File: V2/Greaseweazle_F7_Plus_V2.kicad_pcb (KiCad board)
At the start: 2 copper layers, 80 x 50 mm, 77 parts, among them J1 Wurth 694106301002, J10 PIN1X2, J11 PIN1X2, J12 IDC Box Header, J2 USB_B, J3 Molex 105017-1001, J4 TE EI 171826-4, J5 PIN1X3, J6 PIN1X2, J7 PIN1X5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

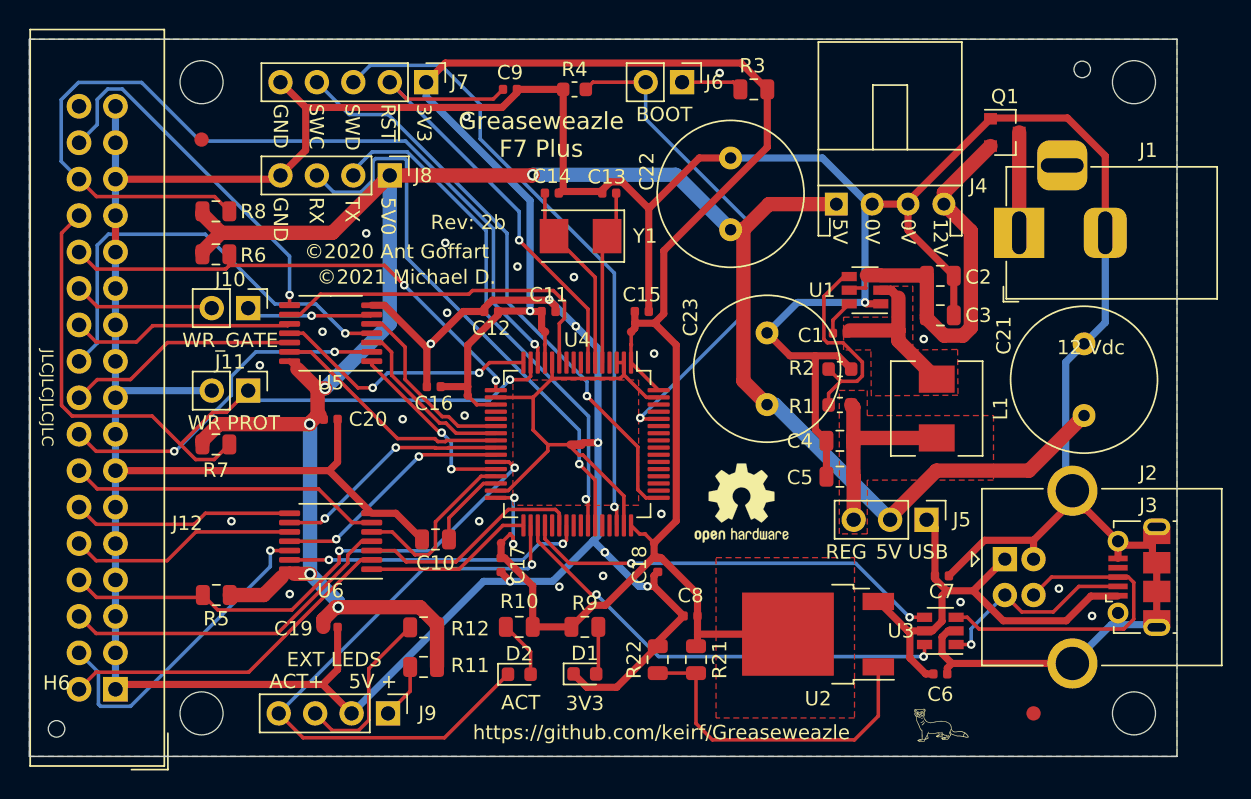
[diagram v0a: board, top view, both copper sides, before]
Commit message: moved U11 NarrowPowCon to get better routing
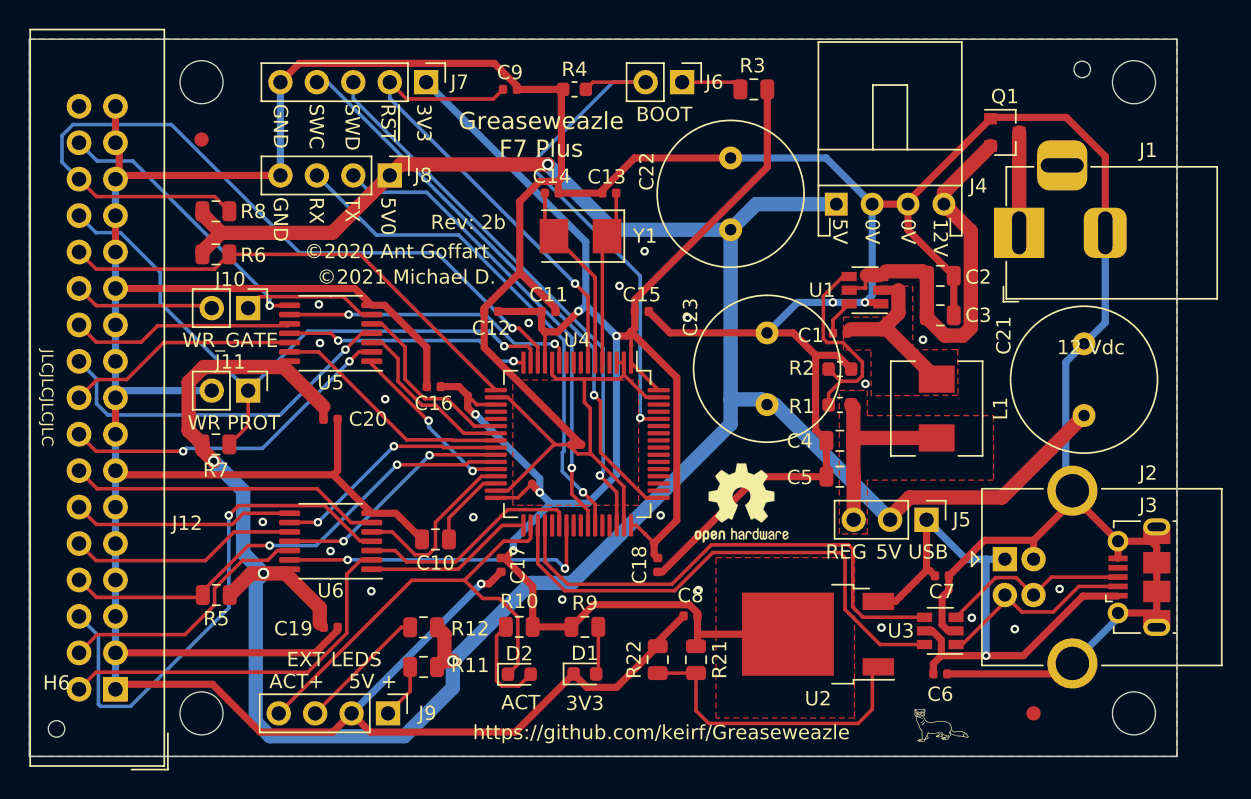
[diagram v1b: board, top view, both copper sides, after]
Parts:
- LOGO2: value Greaseweazle Logo -> GW Logo
- moved U11 4.67 mm to (185.0, 131.0), turned to 315 degrees
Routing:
- net GND: track 389.5 -> 434.8 mm, vias 30 -> 23
- net +5V: track 156.2 -> 192.1 mm, vias 5 -> 4
- net /~PIN6_5V~: track 23.9 -> 36.4 mm, vias 0 -> 1
- net /ACT: track 43.2 -> 32.6 mm, vias 1 -> 0
- net /~WR_PROT~: track 55.3 -> 45.2 mm
- net /USB_DIN+: track 23.2 -> 13.5 mm
- net /~RD_DAT~: track 62.9 -> 55.9 mm
- net /USB_VBUS: track 34.0 -> 40.0 mm, vias 0 -> 1
- net /~SIDE_5V~: track 25.5 -> 19.7 mm
- net /~STEP_5V~: track 30.9 -> 25.3 mm
- net /USB_D+: track 29.7 -> 35.2 mm, vias 2 -> 0
- net /SWDIO: track 43.7 -> 38.7 mm
- net /~PIN4_5V~: track 22.7 -> 18.3 mm, vias 1 -> 0
- net /USB_D-: track 32.2 -> 36.3 mm, vias 2 -> 0
- net /~INDEX~: track 37.4 -> 33.6 mm
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
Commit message: fixed footprint+silk of polarized caps
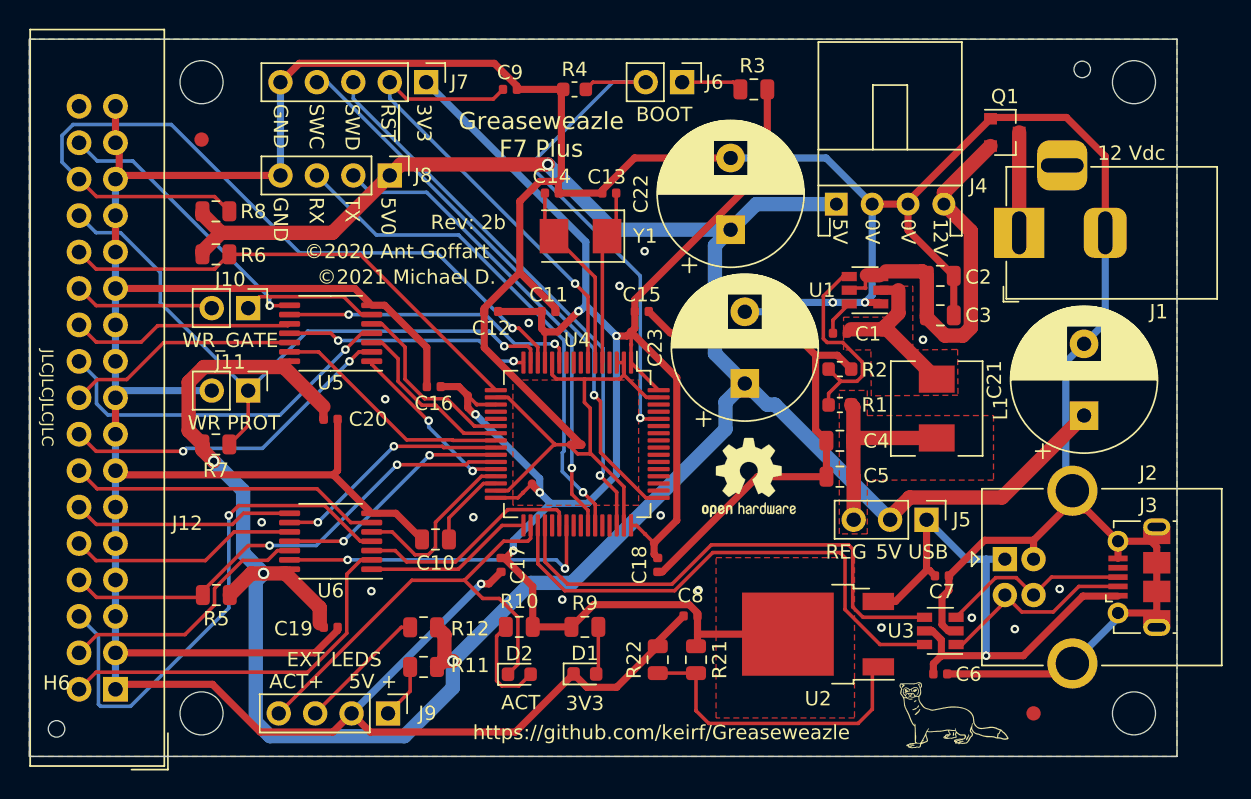
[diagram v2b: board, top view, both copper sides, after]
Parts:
- C21, C22, C23: footprint Capacitor_THT:C_Radial_D10.0mm_H20.0mm_P5.00mm -> Capacitor_THT:CP_Radial_D10.0mm_P5.00mm
- LOGO2: footprint greaseweazle:Greaseweazle_Logo_verysmall -> greaseweazle:Greaseweazle_Logo_small
- moved C23 2.14 mm to (199.9, 124.0)
- moved LOGO1 1.85 mm to (200.2, 130.6)
- moved LOGO2 1.14 mm to (214.5, 147.1)
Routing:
- net +5V: track 192.1 -> 193.3 mm
- net GND: track 434.8 -> 435.8 mm, vias 23 -> 19

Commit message: added silk for powerconn polarity
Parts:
- added REF**: Symbol_Barrel_Polarity, Symbol:Symbol_Barrel_Polarity, F.Cu at (224.9, 105.7)
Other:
- board text added: "-"

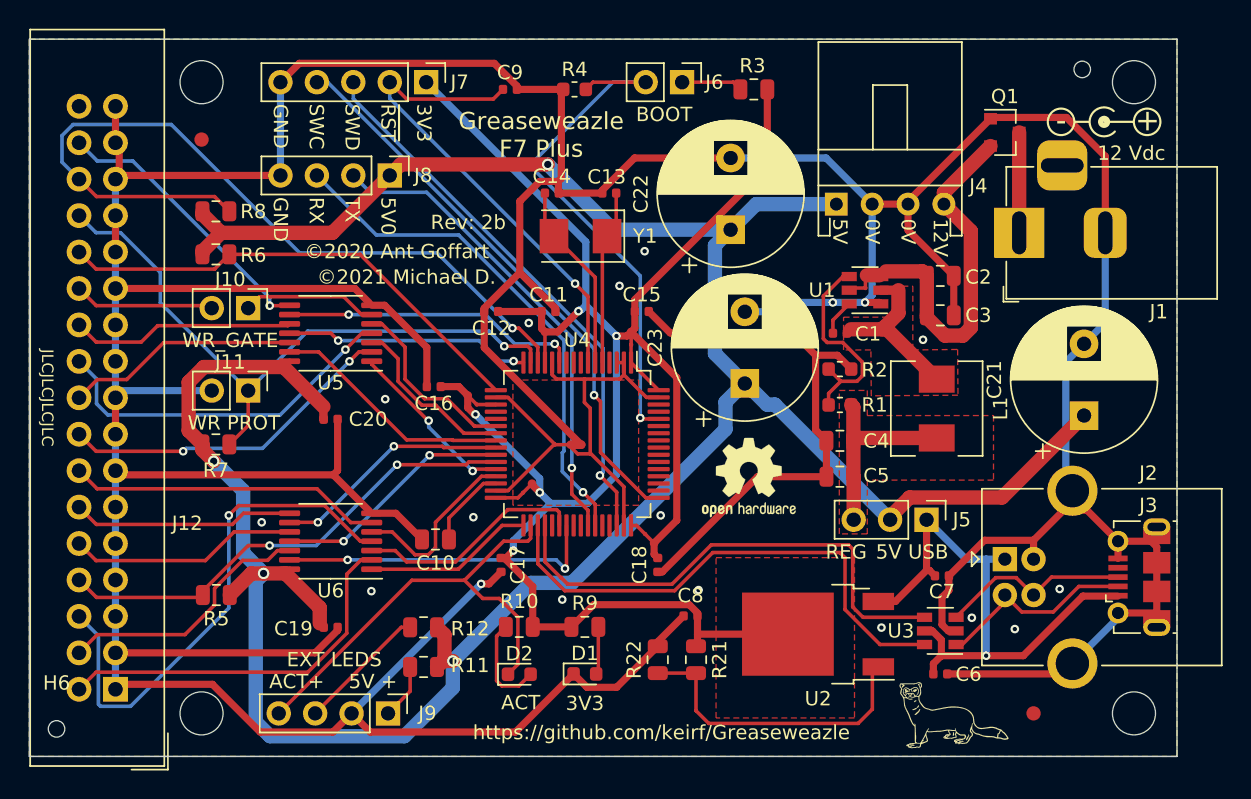
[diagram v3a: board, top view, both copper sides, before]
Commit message: use enhanced floppy interface
use this document as reference: http://www.mcamafia.de/pdf/ps2_fdd_trm_s42g2194_00.pdf
IBM Personal System/2
3.5inch Diskette drives
Technical Reference 42G2194 S42G-2194-00

This version is no longer compatible to original firmware because
some connections changed

support additionally the following pins:
  media type ID 0+1
  drive type ID 0+1
  data rate selection 0+1
  disk change
  +5V (must be set using the "V5 Source" jumper J5)

removed connection from 7407 to pin6 (this is +12V)
pin 4 is now input instead of output
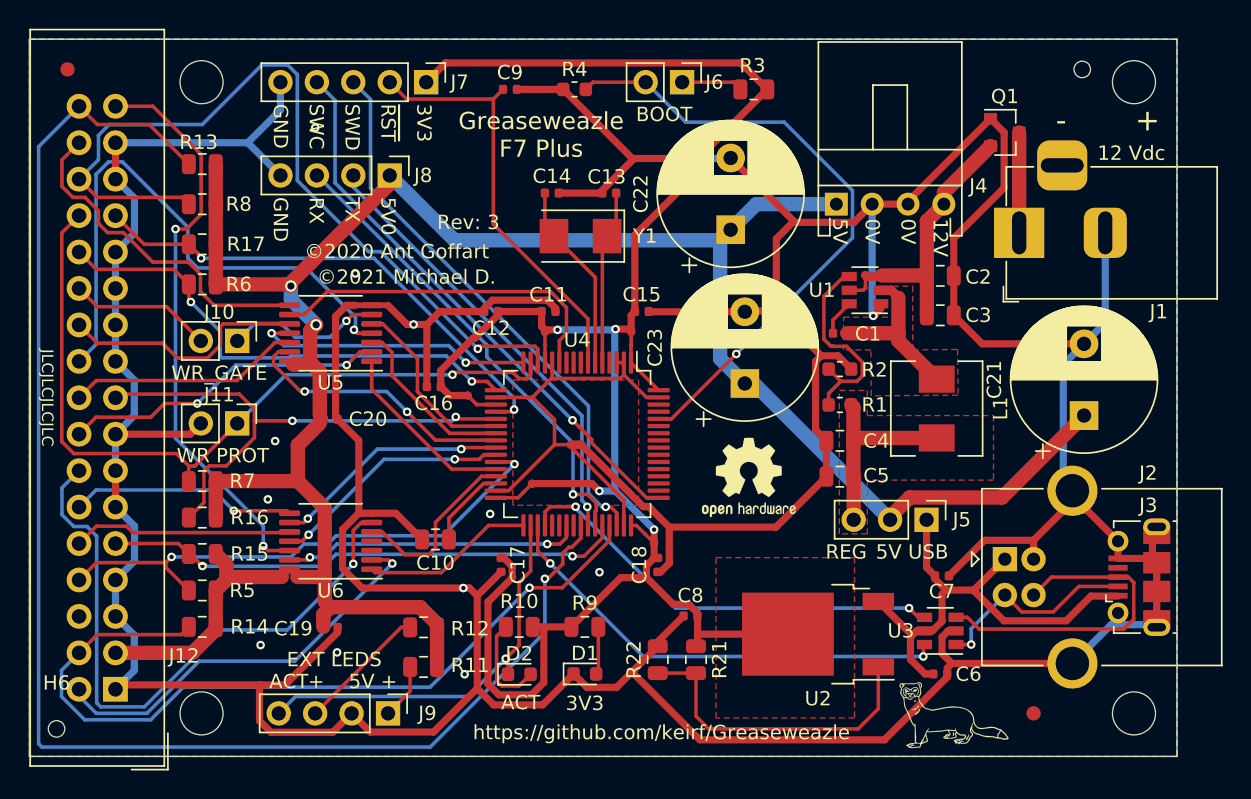
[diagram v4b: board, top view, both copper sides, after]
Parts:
- removed REF**: Symbol_Barrel_Polarity, Symbol:Symbol_Barrel_Polarity
- added R13: 1K0, Resistor_SMD:R_0805_2012Metric, F.Cu at (162.1, 108.7)
- added R14: 1K0, Resistor_SMD:R_0805_2012Metric, F.Cu at (162.1, 141.0)
- added R15: 1K0, Resistor_SMD:R_0805_2012Metric, F.Cu at (162.1, 135.9)
- added R16: 1K0, Resistor_SMD:R_0805_2012Metric, F.Cu at (162.1, 133.3)
- added R17: 1K0, Resistor_SMD:R_0805_2012Metric, F.Cu at (162.1, 114.3)
- moved FID1 10.5 mm to (152.7, 102.1)
- moved R7 2.73 mm to (162.1, 130.8), turned to 180 degrees
- moved J10 2.41 mm to (164.5, 121.0)
- moved J11 2.41 mm to (164.5, 126.8)
- moved R6 2.30 mm to (162.1, 117.1), turned to 180 degrees
- moved R8 1.07 mm to (162.1, 111.5), turned to 180 degrees
- moved R5 1.03 mm to (162.1, 138.4)
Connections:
- net /~PIN2_5V~ renamed /~DATA_RATE_SEL1_5V~
- net /~PIN2~ renamed /~DATA_RATE_SEL1~
- net /~PIN4~ renamed /~DATA_RATE_SEL0~
- J12 pad 17: GND -> /~MTYPE_ID1~
- J12 pad 27: GND -> /~MTYPE_ID0~
- J12 pad 3: GND -> +5V
- J12 pad 33: GND -> /~DATA_RATE_SEL0_5V~
- J12 pad 34: (no net) -> /~DISK_CHANGE~
- J12 pad 4: /~PIN4_5V~ -> /~DTYPE_ID1~
- J12 pad 6: /~PIN6_5V~ -> (no net)
- J12 pad 9: GND -> /~DTYPE_ID0~
- U4 pad 20: (no net) -> /~MTYPE_ID0~
- U4 pad 21: (no net) -> /~MTYPE_ID1~
- U4 pad 38: /~PIN6~ -> (no net)
- U4 pad 41: (no net) -> /~DISK_CHANGE~
- U4 pad 44: (no net) -> /~DTYPE_ID0~
- U4 pad 45: (no net) -> /~DTYPE_ID1~
- U6 pad 12: /~PIN4_5V~ -> /~DATA_RATE_SEL0_5V~
- U6 pad 3: /~PIN6~ -> (no net)
- U6 pad 4: /~PIN6_5V~ -> (no net)
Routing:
- net /~DISK_CHANGE~: track 0.00 -> 102.4 mm, vias 0 -> 1
- net /~DTYPE_ID1~: track 0.00 -> 57.1 mm, vias 0 -> 1
- net /~DATA_RATE_SEL0_5V~: track 0.00 -> 40.3 mm, vias 0 -> 2
- net /~MTYPE_ID1~: track 0.00 -> 37.4 mm, vias 0 -> 2
- net /~PIN6_5V~: track 36.4 -> 0.00 mm, vias 1 -> 0
- net /~DTYPE_ID0~: track 0.00 -> 36.4 mm, vias 0 -> 2
- net /~MTYPE_ID0~: track 0.00 -> 35.3 mm, vias 0 -> 2
- net +5V: track 193.3 -> 168.2 mm, vias 4 -> 2
- net /~DS0_5V~: track 21.9 -> 44.2 mm, vias 0 -> 1
- net /~PIN4_5V~: track 18.3 -> 0.00 mm
- net GND: track 435.8 -> 417.8 mm, vias 19 -> 13
- net /~PIN6~: track 15.9 -> 0.00 mm
- net /~STEP_5V~: track 25.3 -> 40.0 mm
- net /USB_DIN+: track 13.5 -> 23.2 mm
- net /~WR_PROT~: track 45.2 -> 54.5 mm
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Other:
- board text added: "Rev: 3"
- board text removed: "Rev: 2b"

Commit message: moved components to optimize routing
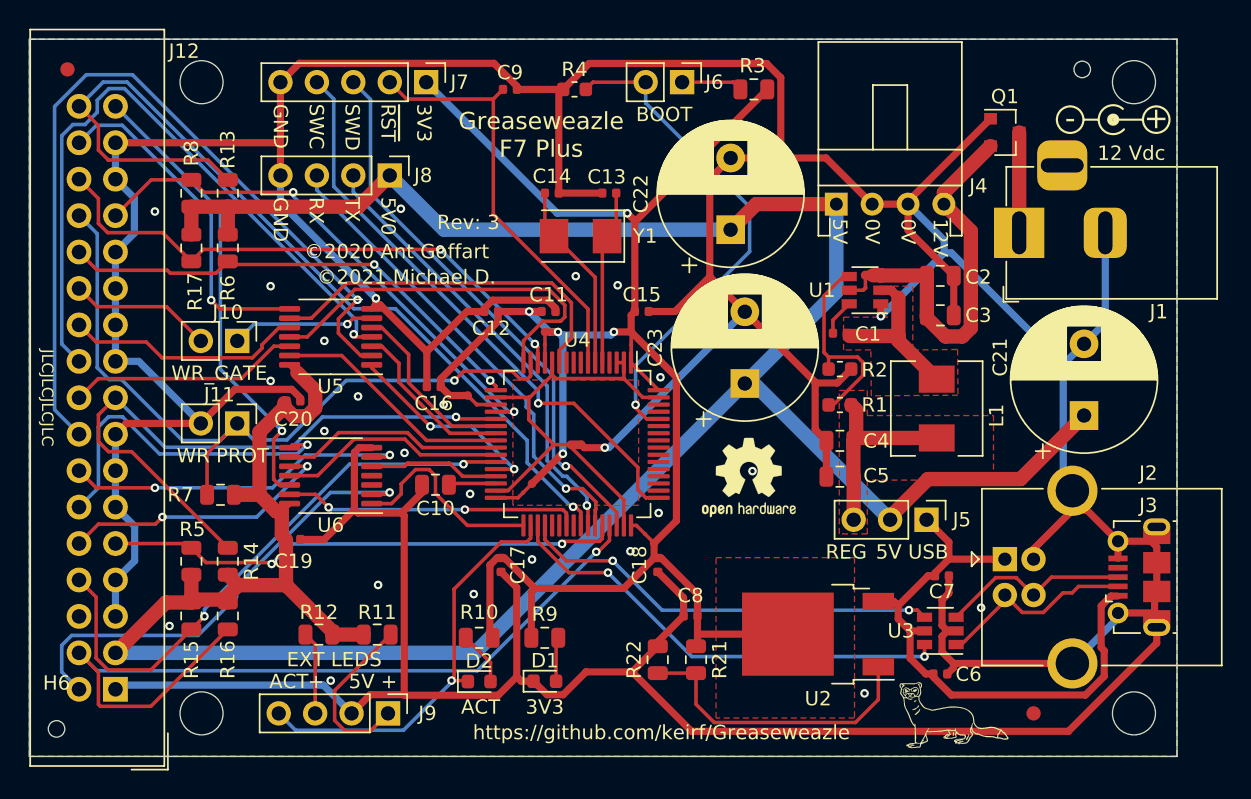
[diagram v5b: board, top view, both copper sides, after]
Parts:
- added LOGO3: GW Logo, Symbol:Symbol_Barrel_Polarity, F.Cu at (225.6, 105.5)
- moved R12 7.32 mm to (170.2, 141.5)
- moved C19 6.65 mm to (168.4, 134.9)
- moved U6 4.57 mm to (171.0, 130.4)
- moved R11 3.94 mm to (174.2, 141.5), turned to 0 degrees
- moved C10 3.81 mm to (178.3, 131.1)
- moved R17 3.64 mm to (161.3, 110.7), turned to 270 degrees
- moved R16 3.53 mm to (163.8, 136.4), turned to 270 degrees
- moved R8 3.14 mm to (161.3, 114.6), turned to 270 degrees
- moved R6 3.10 mm to (163.8, 114.6), turned to 270 degrees
- moved R10 2.90 mm to (181.4, 141.7)
- moved R9 2.90 mm to (185.9, 141.7)
- moved C20 2.90 mm to (168.4, 125.2)
- moved D1 2.84 mm to (185.9, 144.8)
- moved D2 2.84 mm to (181.4, 144.8)
- moved R13 2.70 mm to (163.8, 110.7), turned to 90 degrees
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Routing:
- net /~DISK_CHANGE~: track 102.4 -> 63.4 mm
- net /~M1_5V~: track 22.8 -> 57.9 mm, vias 2 -> 1
- net GND: track 417.8 -> 449.7 mm, vias 13 -> 26
- net +5V: track 168.2 -> 196.9 mm, vias 2 -> 0
- net /~DS0_5V~: track 44.2 -> 24.4 mm, vias 1 -> 2
- net /~RD_DAT~: track 58.3 -> 39.6 mm, vias 1 -> 2
- net /USB_DIN+: track 23.2 -> 13.5 mm
- net /BOOT: track 44.0 -> 35.3 mm
- net Net-(J9-Pad1): track 3.87 -> 12.1 mm
- net /~DATA_RATE_SEL0_5V~: track 40.3 -> 32.3 mm, vias 2 -> 1
- net +12V: track 18.0 -> 26.0 mm
- net /~DS1_5V~: track 15.8 -> 23.7 mm
- net /~STEP_5V~: track 40.0 -> 47.7 mm
- net /~WR_DAT~: track 19.7 -> 26.9 mm, vias 2 -> 0
- net /~MTYPE_ID1~: track 37.4 -> 44.5 mm, vias 2 -> 1
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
